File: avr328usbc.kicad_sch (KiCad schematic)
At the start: 18 parts, among them J1 USB-C THT, J2 MCP Debug Header, J3 USB-C THT, U1 MCP2221AxP, U2 ACPL-772L-000E, U3 ACPL-772L-000E

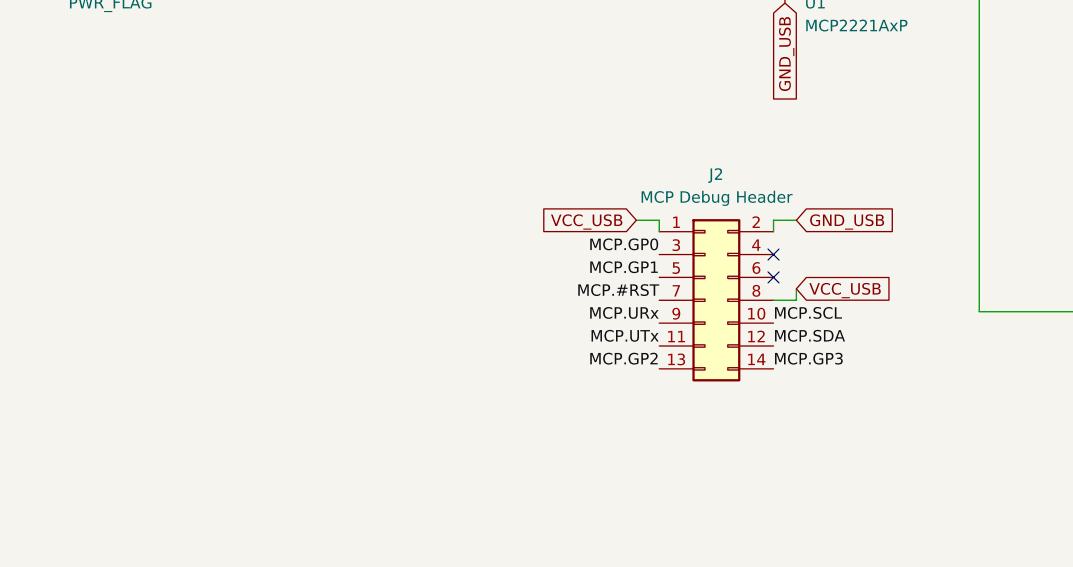
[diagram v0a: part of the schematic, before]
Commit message: changed MCP header into two headers mirroring part
also rearanged components on board
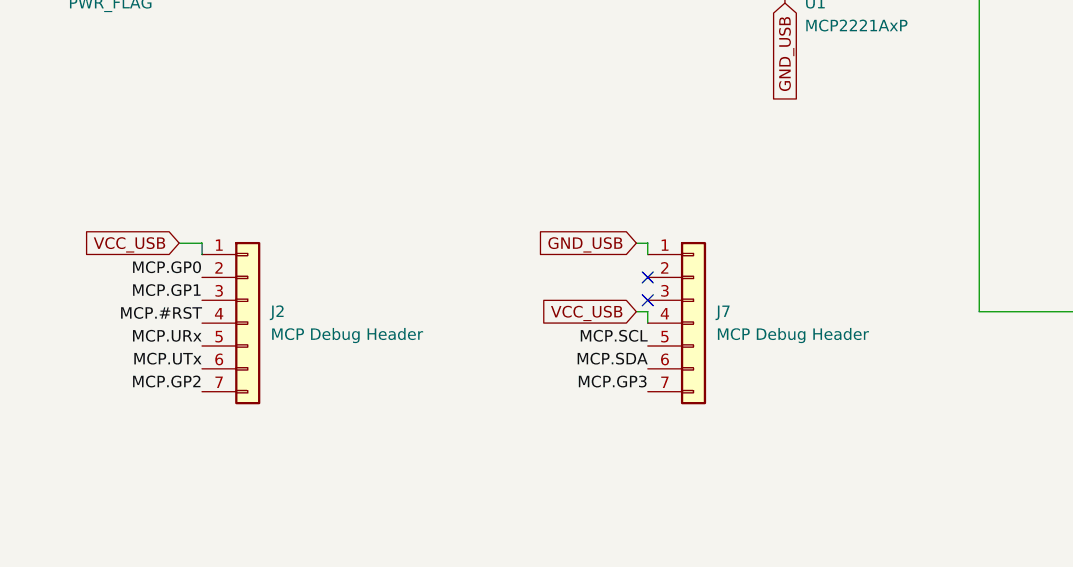
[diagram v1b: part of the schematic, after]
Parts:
- added J7: MCP Debug Header, Connector_PinHeader_2.54mm:PinHeader_1x07_P2.54mm_Vertical, symbol Connector_Generic:Conn_01x07
- J2: footprint Connector_PinHeader_2.54mm:PinHeader_2x07_P2.54mm_Vertical -> Connector_PinHeader_2.54mm:PinHeader_1x07_P2.54mm_Vertical; symbol Connector_Generic:Conn_02x07_Odd_Even -> Connector_Generic:Conn_01x07; MFR Amphenol -> TE Connectivity; MFR Part Num (none) -> 825433-7
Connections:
- net GND_USB: now also J7.1 (Pin_1); no longer J2.2 (Pin_2)
- net MCP.#RST: now also J2.4 (Pin_4); no longer J2.7 (Pin_7)
- net MCP.GP0: now also J2.2 (Pin_2); no longer J2.3 (Pin_3)
- net MCP.GP1: now also J2.3 (Pin_3); no longer J2.5 (Pin_5)
- net MCP.GP2: now also J2.7 (Pin_7); no longer J2.13 (Pin_13)
- net MCP.GP3: now also J7.7 (Pin_7); no longer J2.14 (Pin_14)
- net MCP.SCL: now also J7.5 (Pin_5); no longer J2.10 (Pin_10)
- net MCP.SDA: now also J7.6 (Pin_6); no longer J2.12 (Pin_12)
- net MCP.URx: now also J2.5 (Pin_5); no longer J2.9 (Pin_9)
- net MCP.UTx: now also J2.6 (Pin_6); no longer J2.11 (Pin_11)
- net VCC_USB: now also J7.4 (Pin_4); no longer J2.8 (Pin_8)

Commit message: modified USB-C footprint to follow clearence rules at OSH
Now almost all DRCs pass
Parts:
- J1, J3: footprint Connector_USB:USB_C_Receptacle_GCT_USB4085 -> AAAA_Project_Library:USB_C_Receptacle_GCT_USB4085_Reduced_Pad_Size
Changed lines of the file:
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@@
 			)
 		)
-		(property "Footprint" "Connector_USB:USB_C_Receptacle_GCT_USB4085"
+		(property "Footprint" "AAAA_Project_Library:USB_C_Receptacle_GCT_USB4085_Reduced_Pad_Size"
 			(at 34.29 55.88 0)
 			(effects
@@
 			)
 		)
-		(property "Footprint" "Connector_USB:USB_C_Receptacle_GCT_USB4085"
+		(property "Footprint" "AAAA_Project_Library:USB_C_Receptacle_GCT_USB4085_Reduced_Pad_Size"
 			(at 209.55 81.28 0)
 			(effects
